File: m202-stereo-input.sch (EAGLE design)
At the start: 77 parts, among them U1 SCREW-M2X8, U10 FX2-20S-1.27DS, U11 ERM1-5MM, U2 SCREW-M2X8, U3 NUT-M2-SELFLOCK, U4 NUT-M2-SELFLOCK, U5 FX2-20P-1.27DS, U6 SCREW-M2X8, U7 SCREW-M2X8, U8 NUT-M2-SELFLOCK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

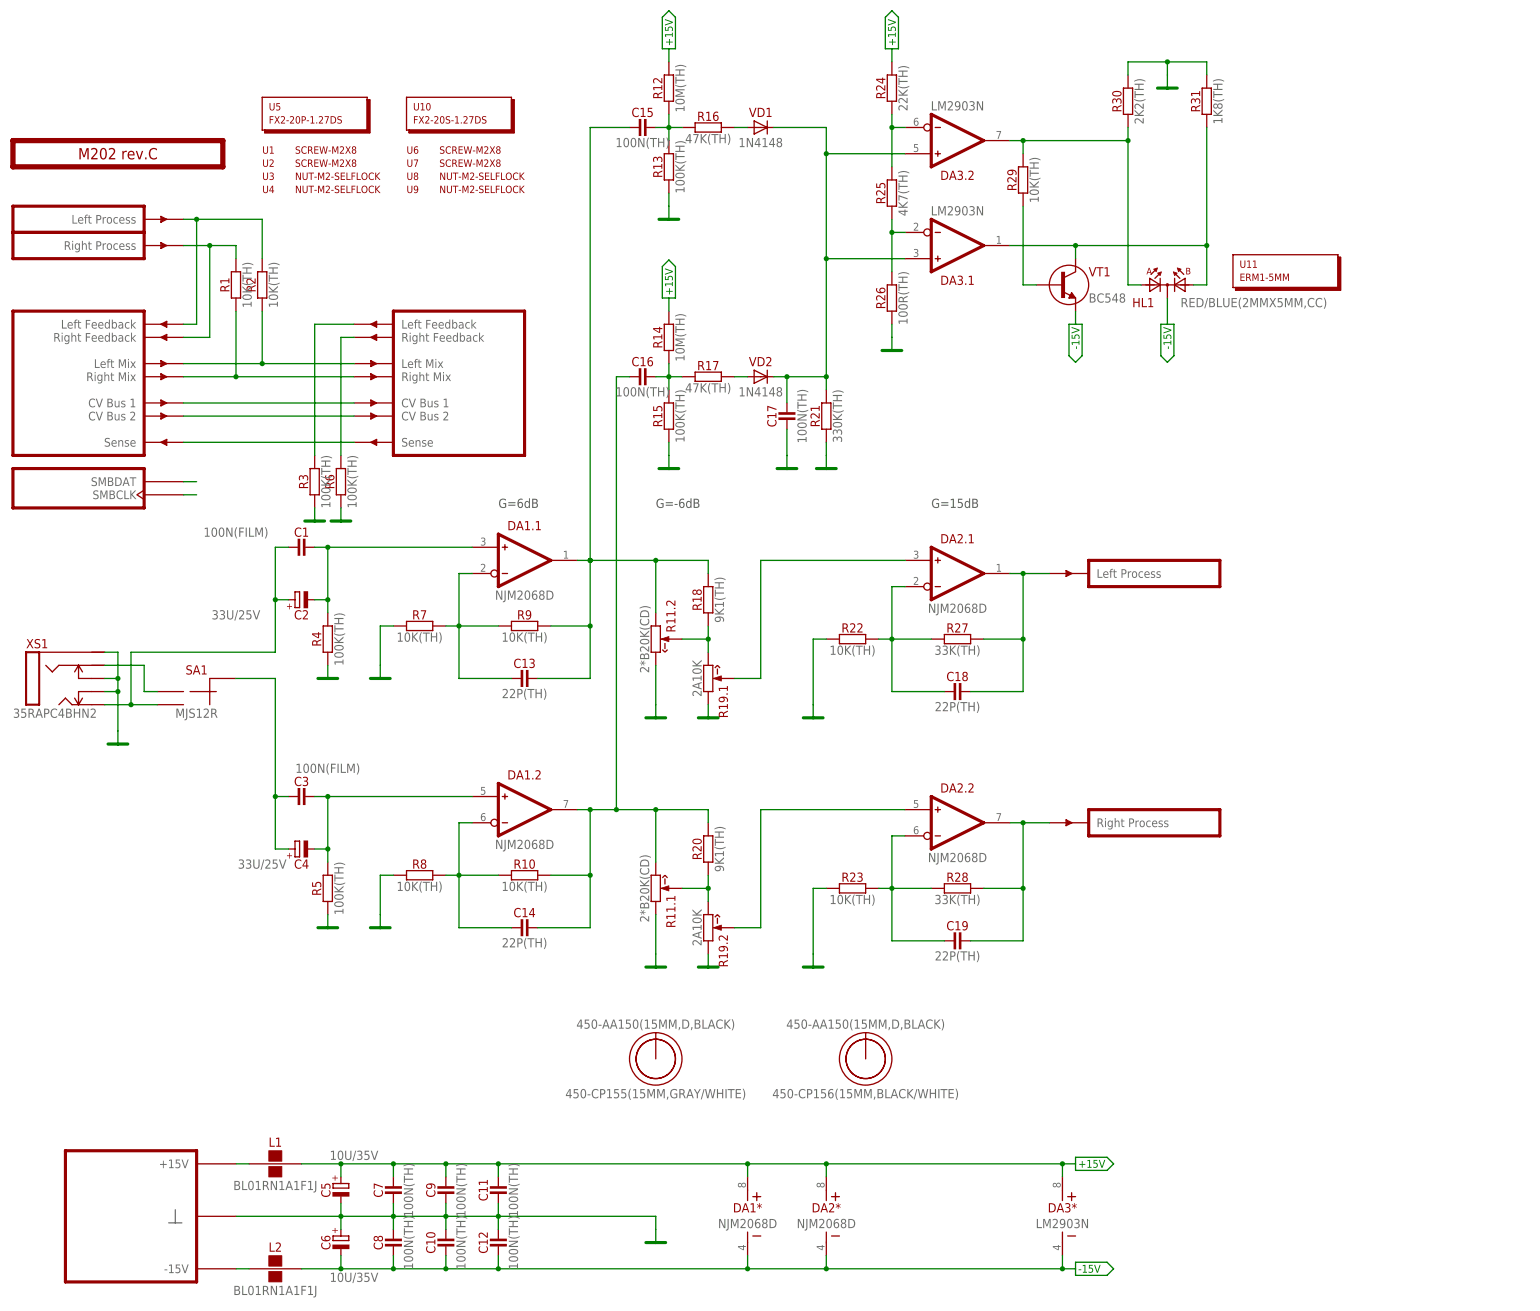
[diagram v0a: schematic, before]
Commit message: M202d: Improved signal indicator
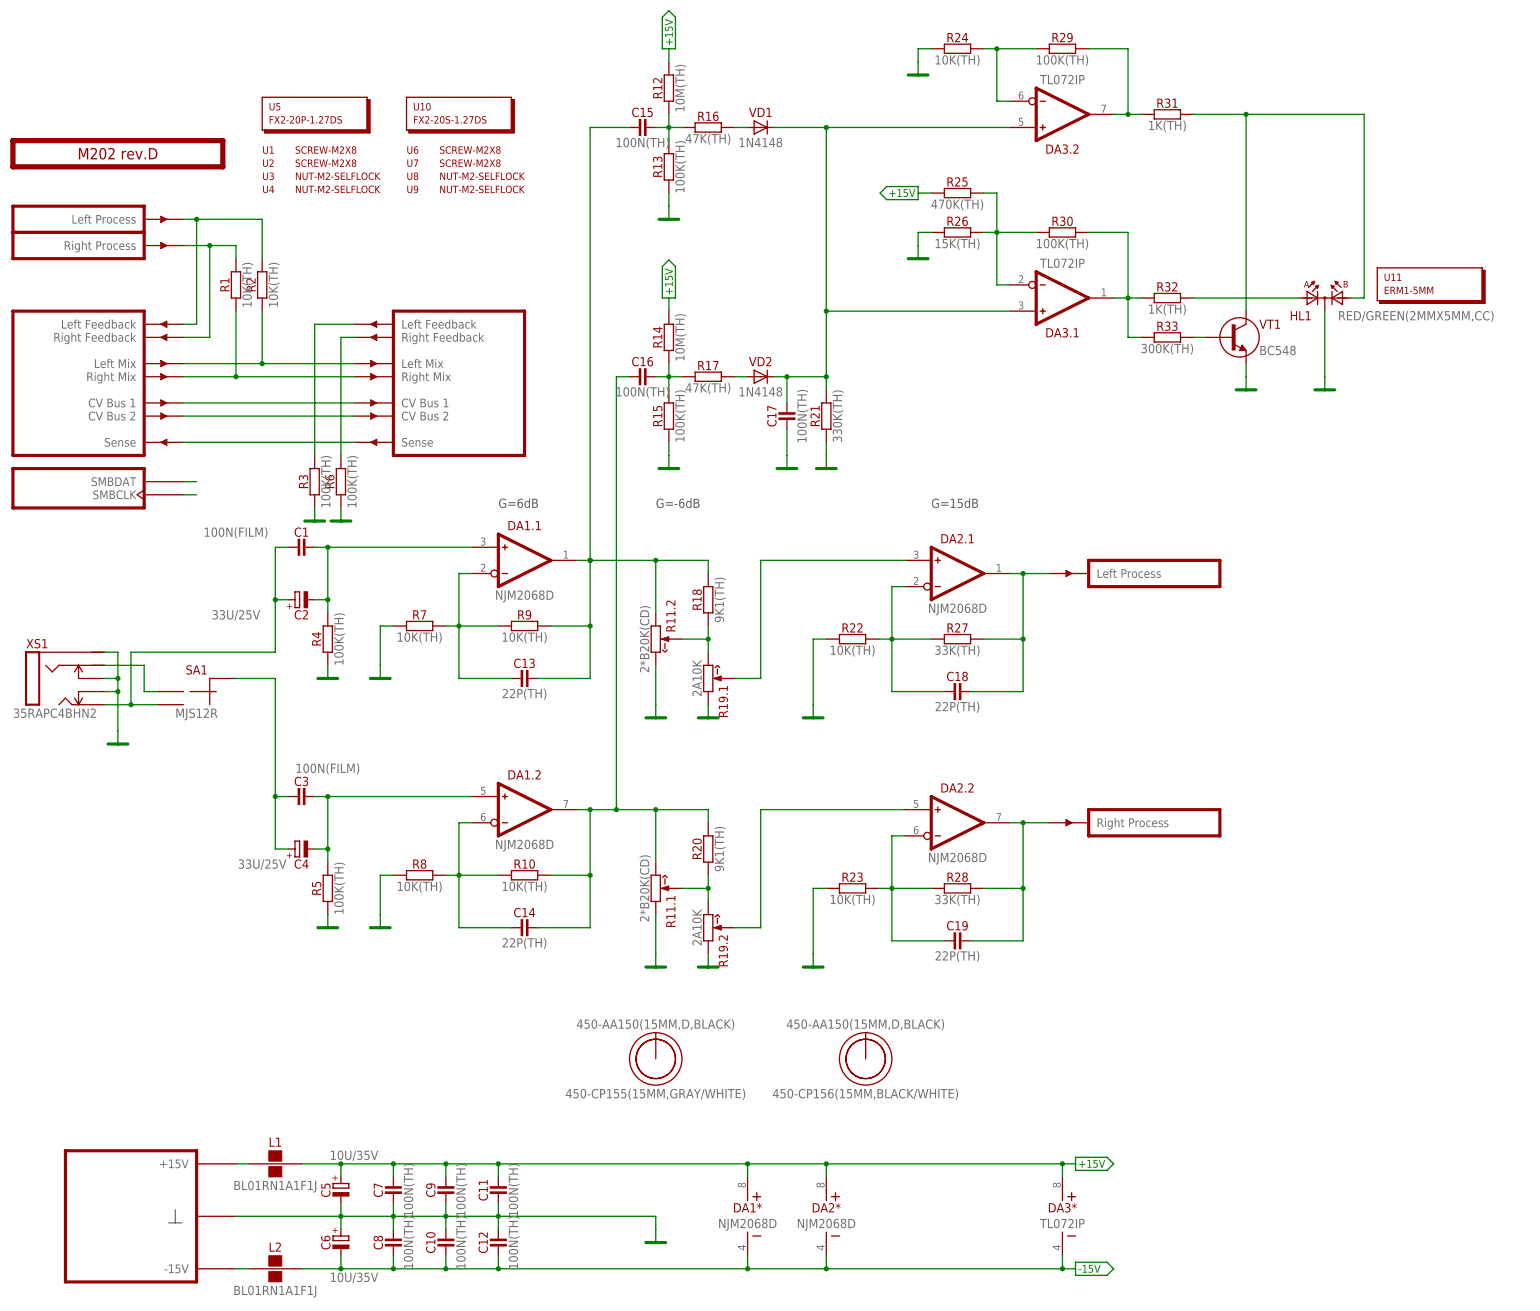
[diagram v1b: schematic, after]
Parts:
- added R32: 1K(TH), resistors:1K(TH)
- added R33: 300K(TH), resistors:300K(TH)
- DA3: value LM2903N -> TL072IP; device ic-fairchild:LM2903N -> ic-ti:TL072IP
- HL1: value RED/BLUE(2MMX5MM,CC) -> RED/GREEN(2MMX5MM,CC); device optoelectronics:RED/BLUE(2MMX5MM,CC) -> optoelectronics:RED/GREEN(2MMX5MM,CC)
- PCB1: value M202 rev.C -> M202 rev.D
- R24: value 22K(TH) -> 10K(TH); device resistors:22K(TH) -> resistors:10K(TH)
- R25: value 4K7(TH) -> 470K(TH); device resistors:4K7(TH) -> resistors:470K(TH)
- R26: value 100R(TH) -> 15K(TH); device resistors:100R(TH) -> resistors:15K(TH)
- R29: value 10K(TH) -> 100K(TH); device resistors:10K(TH) -> resistors:100K(TH)
- R30: value 2K2(TH) -> 100K(TH); device resistors:2K2(TH) -> resistors:100K(TH)
- R31: value 1K8(TH) -> 1K(TH); device resistors:1K8(TH) -> resistors:1K(TH)
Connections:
- removed net N$46: DA3.1.IN-, R25.1, R26.2
- removed net N$47: DA3.2.IN-, R24.1, R25.2
- removed net N$48: DA3.2.OUT, HL1.A1, R29.2, R30.1
- removed net N$49: R29.1, VT1.B
- removed net N$51: DA3.1.OUT, HL1.A2, R31.1, VT1.C
- new net N$18: DA3.2.IN-, R24.2, R29.1
- new net N$20: DA3.2.OUT, R29.2, R31.1
- new net N$21: HL1.A2, R31.2, VT1.C
- new net N$22: DA3.1.IN-, R25.2, R26.2, R30.1
- new net N$23: DA3.1.OUT, R30.2, R32.1, R33.1
- new net N$25: R33.2, VT1.B
- new net N$33: HL1.A1, R32.2
- net +15V: now also R25.1; no longer R24.2
- net -15V: no longer HL1.K, VT1.E
- net GND: now also HL1.K, R24.1, VT1.E; no longer R30.2, R31.2
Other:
- moved on the sheet: DA3.1, DA3.2, HL1, R24, R25, R26, R29, R30, R31, U11, VT1

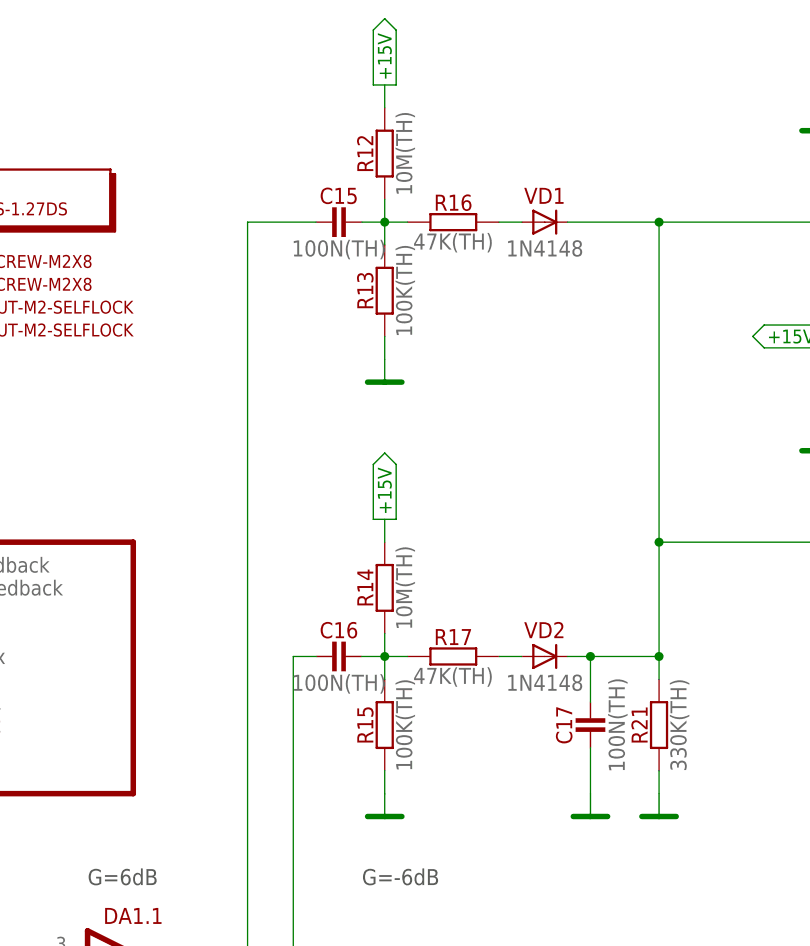
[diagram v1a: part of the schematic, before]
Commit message: M202d: Resistor values fix
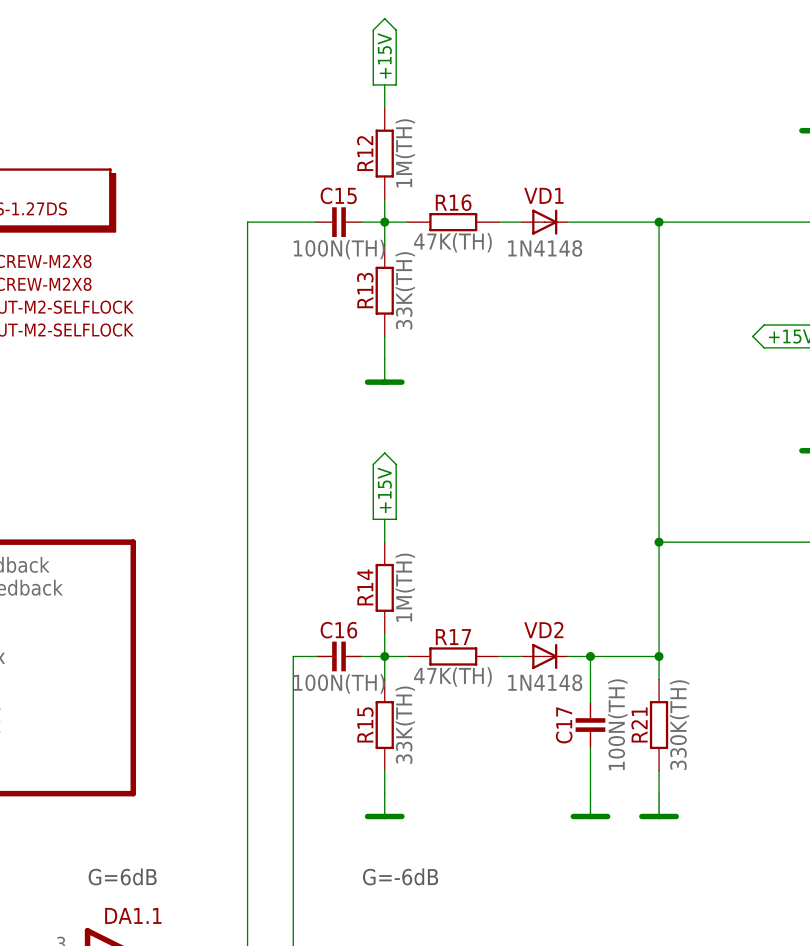
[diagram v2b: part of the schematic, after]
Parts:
- R12, R14: value 10M(TH) -> 1M(TH); device resistors:10M(TH) -> resistors:1M(TH)
- R13, R15: value 100K(TH) -> 33K(TH); device resistors:100K(TH) -> resistors:33K(TH)
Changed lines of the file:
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@@
 <part name="C15" library="capacitors" deviceset="?" device="100N(TH)" value="100N(TH)"/>
 <part name="C16" library="capacitors" deviceset="?" device="100N(TH)" value="100N(TH)"/>
-<part name="R12" library="resistors" deviceset="?" device="10M(TH)" value="10M(TH)"/>
-<part name="R14" library="resistors" deviceset="?" device="10M(TH)" value="10M(TH)"/>
-<part name="R13" library="resistors" deviceset="?" device="100K(TH)" value="100K(TH)"/>
-<part name="R15" library="resistors" deviceset="?" device="100K(TH)" value="100K(TH)"/>
+<part name="R12" library="resistors" deviceset="?" device="1M(TH)" value="1M(TH)"/>
+<part name="R14" library="resistors" deviceset="?" device="1M(TH)" value="1M(TH)"/>
+<part name="R13" library="resistors" deviceset="?" device="33K(TH)" value="33K(TH)"/>
+<part name="R15" library="resistors" deviceset="?" device="33K(TH)" value="33K(TH)"/>
 <part name="R16" library="resistors" deviceset="?" device="47K(TH)" value="47K(TH)"/>
 <part name="R17" library="resistors" deviceset="?" device="47K(TH)" value="47K(TH)"/>

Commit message: M202d Resistor Value Update
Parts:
- R33: value 300K(TH) -> 330K(TH); device resistors:300K(TH) -> resistors:330K(TH)
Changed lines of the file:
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@@
 <part name="R26" library="resistors" deviceset="?" device="15K(TH)"/>
 <part name="R25" library="resistors" deviceset="?" device="470K(TH)"/>
-<part name="R33" library="resistors" deviceset="?" device="300K(TH)"/>
+<part name="R33" library="resistors" deviceset="?" device="330K(TH)" value="330K(TH)"/>
 <part name="R32" library="resistors" deviceset="?" device="1K(TH)"/>
 <part name="R31" library="resistors" deviceset="?" device="1K(TH)"/>
